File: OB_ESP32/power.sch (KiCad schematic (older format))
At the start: 45 parts, among them U1 V3S, U2 EA3058

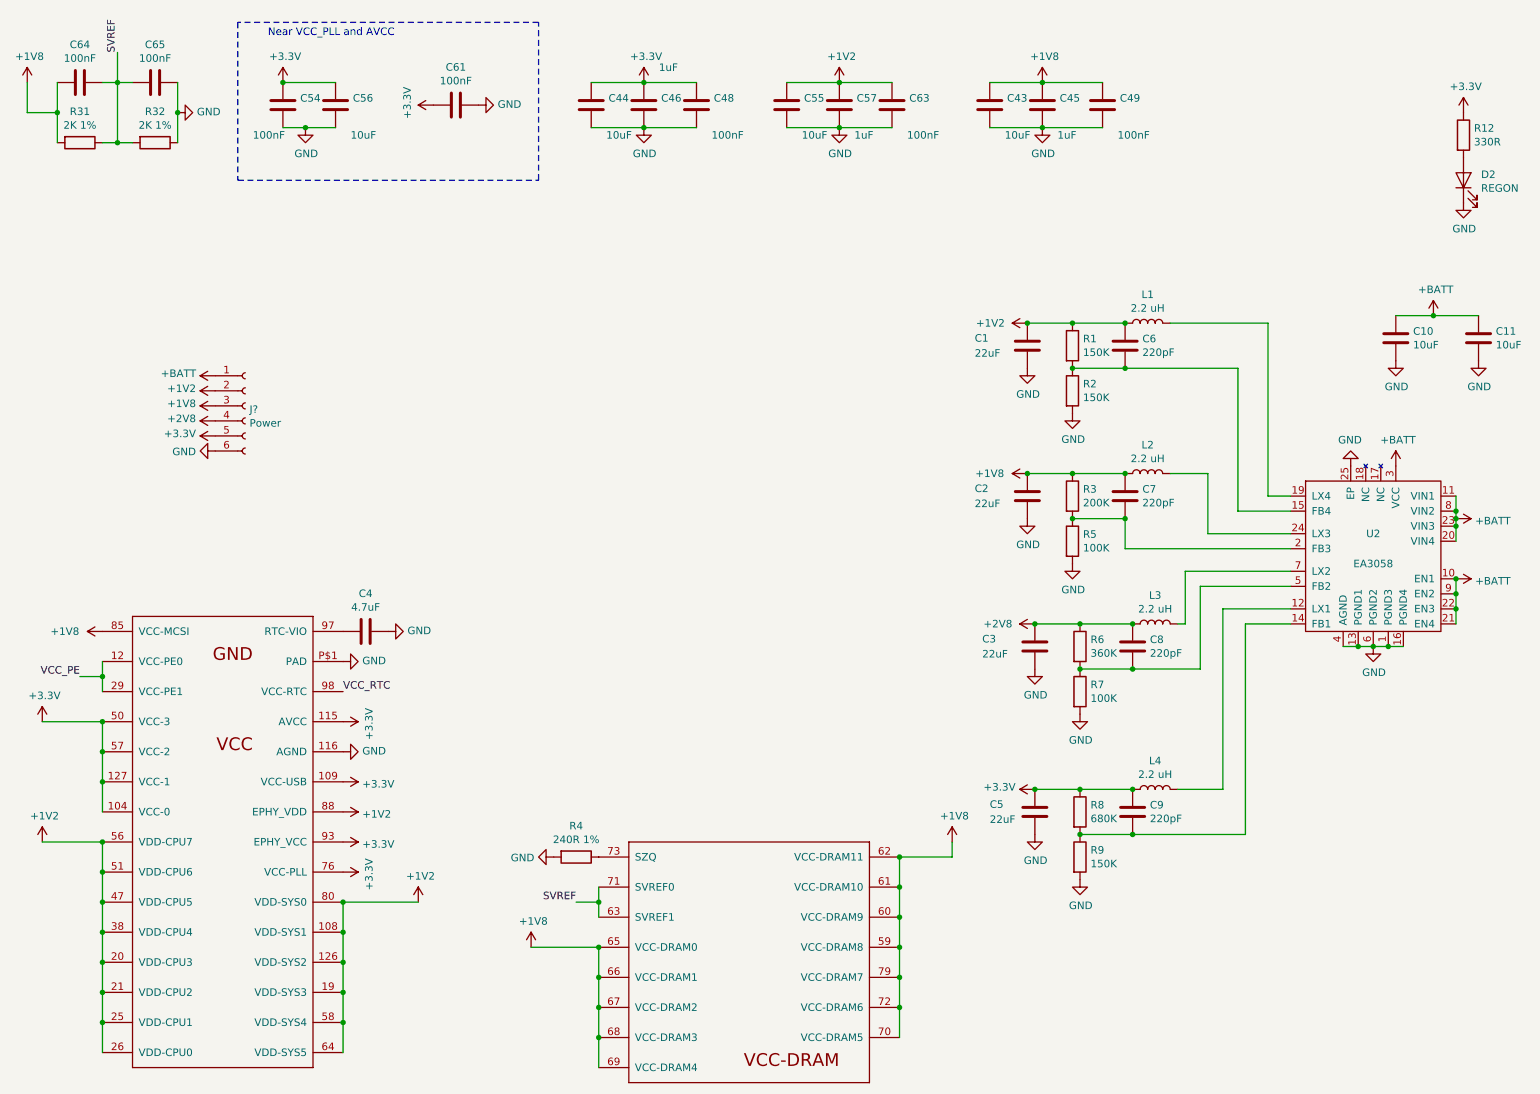
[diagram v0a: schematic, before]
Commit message: +esp32picod4 +fix mounting hole position -ceramic antenna +ufl -spi flash
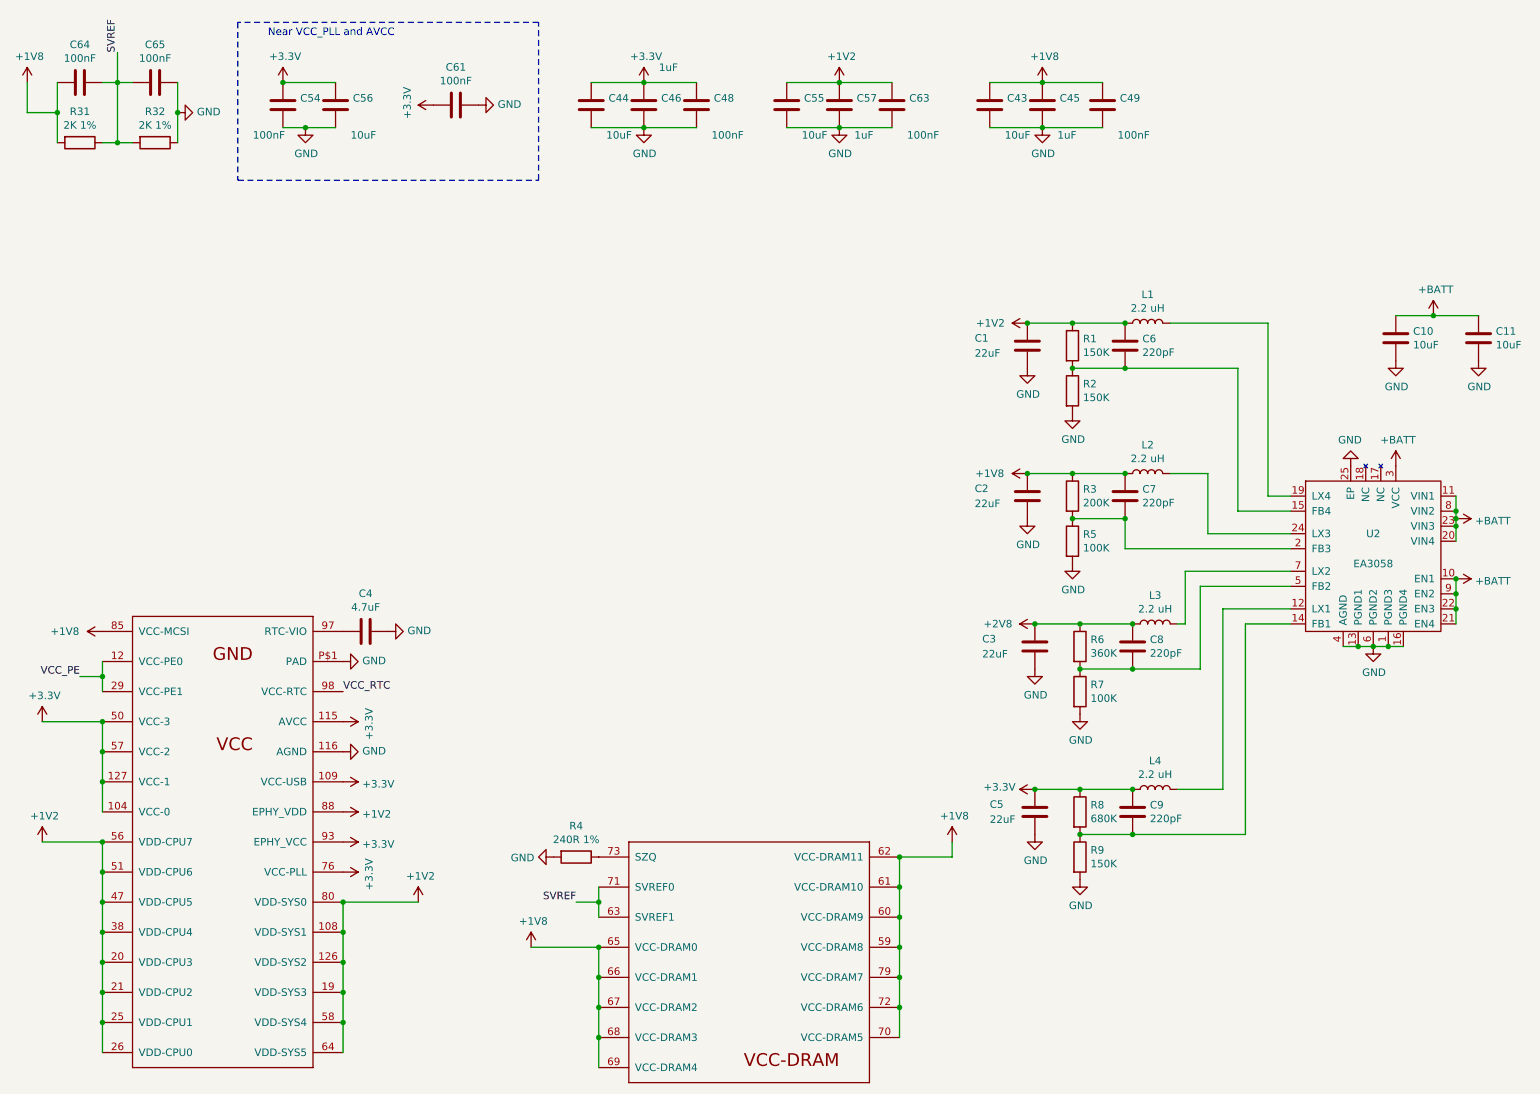
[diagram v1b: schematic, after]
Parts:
- removed D2: REGON, LED_SMD:LED_0402_1005Metric, symbol Device:LED
- removed J?: Power, symbol Connector:Conn_01x06_Female
- removed R12: 330R, Resistor_SMD:R_0402_1005Metric, symbol Device:R
- C1, C10, C11, C2, C3, C4, C43, C44, C45, C46, C5, C55, C56, C57, C6, C7, C8, C9: footprint Capacitor_SMD:C_0402_1005Metric -> Capacitor_SMD:C_0201_0603Metric
- R1, R2, R3, R31, R32, R4, R5, R6, R7, R8, R9: footprint Resistor_SMD:R_0402_1005Metric -> Resistor_SMD:R_0201_0603Metric
- U2: footprint (none) -> Housings_DFN_QFN:QFN-24-1EP_4x4mm_Pitch0.5mm
